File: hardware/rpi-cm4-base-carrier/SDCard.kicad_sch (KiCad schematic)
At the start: 6 parts, among them J6 Micro_SD_Card_Det, U6 RT9742GGJ5

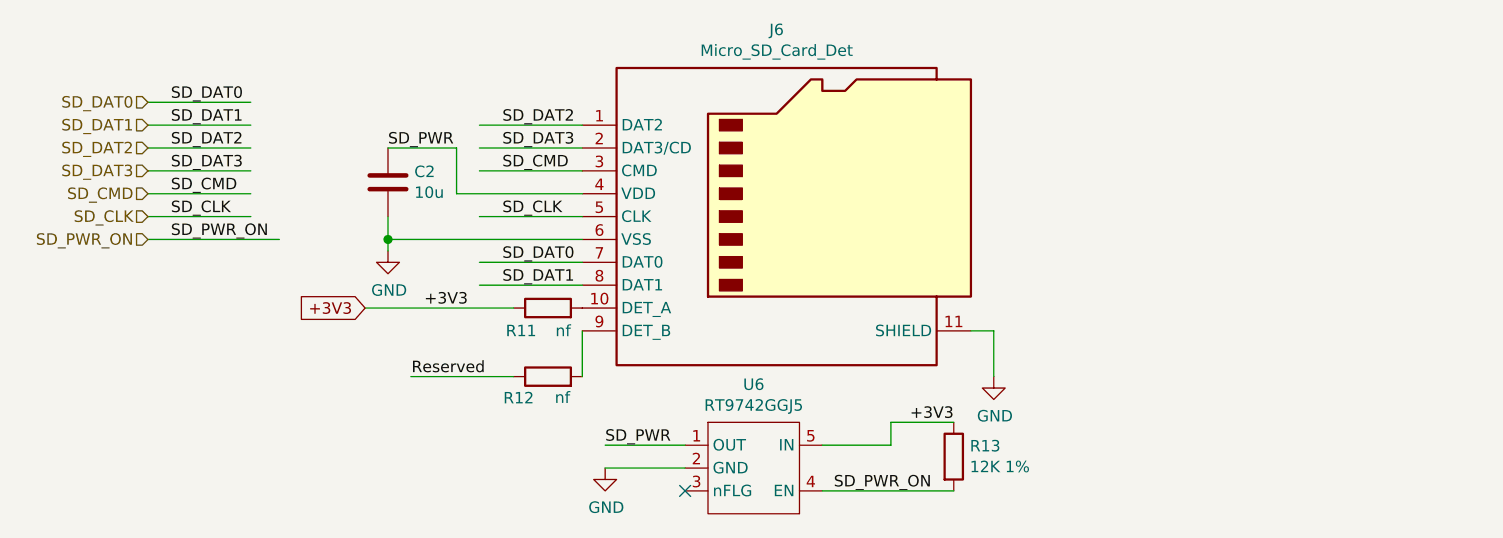
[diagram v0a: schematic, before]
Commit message: routing for some modules progressing quickly, USBHUB mostly complete, thought needed regarding which connectors should be exposed post assembly and which should be for internal use only. LED identifiers and buttons still missing
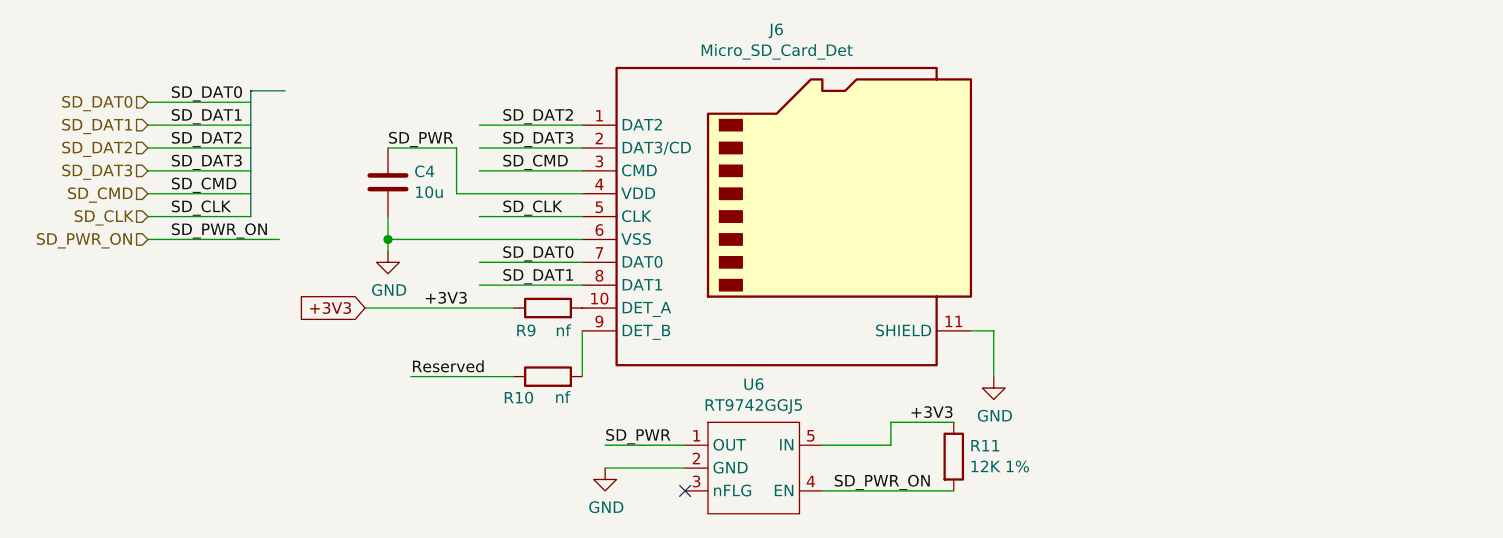
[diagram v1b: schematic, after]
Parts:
- renumbered C2 to C4, R12 to R10, R13 to R11, R11 to R9
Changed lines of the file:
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@@
     (stroke (width 0) (type solid))
+  )
+  (bus (pts (xy 54.61 24.13) (xy 50.8 24.13))
+    (stroke (width 0) (type default))
   )
   (wire (pts (xy 39.37 27.94) (xy 50.8 27.94))
@@
     (stroke (width 0) (type solid))
   )
+  (bus (pts (xy 50.8 24.13) (xy 50.8 38.1))
+    (stroke (width 0) (type default))
+  )
   (label "SD_PWR_ON" (at 41.91 40.64 0) (fields_autoplaced)
     (effects (font (size 1.27 1.27)) (justify left bottom))
@@
     (effects (font (size 1.27 1.27)) (justify right))
   )
+  (netclass_flag "" (length 2.54) (shape round) (at 54.61 24.13 0) (fields_autoplaced)
+    (effects (font (size 1.27 1.27)) (justify left bottom))
+    (property "Netclass" "SD 50R Single" (at 55.499 21.59 0)
+      (effects (font (size 1.27 1.27) italic) (justify left))
+    )
+  )
   (symbol (lib_id "Device:R") (at 83.82 55.88 90) (unit 1)
     (in_bom yes) (on_board yes) (dnp no)
-    (property "Reference" "R12" (at 82.2706 58.2676 90)
+    (property "Reference" "R10" (at 82.2706 58.2676 90)
       (effects (font (size 1.27 1.27)) (justify left))
     )
@@
       (project "rpi-cm4-base-carrier"
         (path "/92c58705-ecb0-498b-b561-44a3f0daad57/26b25ff9-f711-41bc-bcf8-c3ce0c6a0e37"
-          (reference "R12") (unit 1)
+          (reference "R10") (unit 1)
         )
       )
@@
   (symbol (lib_id "power:GND") (at 133.35 55.88 0) (unit 1)
     (in_bom yes) (on_board yes) (dnp no)
-    (property "Reference" "#PWR07" (at 133.35 62.23 0)
+    (property "Reference" "#PWR023" (at 133.35 62.23 0)
       (effects (font (size 1.27 1.27)) hide)
     )
@@
       (project "rpi-cm4-base-carrier"
         (path "/92c58705-ecb0-498b-b561-44a3f0daad57/26b25ff9-f711-41bc-bcf8-c3ce0c6a0e37"
-          (reference "#PWR07") (unit 1)
+          (reference "#PWR023") (unit 1)
         )
       )
@@
   (symbol (lib_id "power:GND") (at 66.04 41.91 0) (unit 1)
     (in_bom yes) (on_board yes) (dnp no)
-    (property "Reference" "#PWR05" (at 66.04 48.26 0)
+    (property "Reference" "#PWR021" (at 66.04 48.26 0)
       (effects (font (size 1.27 1.27)) hide)
     )
@@
       (project "rpi-cm4-base-carrier"
         (path "/92c58705-ecb0-498b-b561-44a3f0daad57/26b25ff9-f711-41bc-bcf8-c3ce0c6a0e37"
-          (reference "#PWR05") (unit 1)
+          (reference "#PWR021") (unit 1)
         )
       )
@@
   (symbol (lib_id "Device:R") (at 83.82 48.26 90) (unit 1)
     (in_bom yes) (on_board yes) (dnp no)
-    (property "Reference" "R11" (at 82.55 50.8 90)
+    (property "Reference" "R9" (at 82.55 50.8 90)
       (effects (font (size 1.27 1.27)) (justify left))
     )
@@
       (project "rpi-cm4-base-carrier"
         (path "/92c58705-ecb0-498b-b561-44a3f0daad57/26b25ff9-f711-41bc-bcf8-c3ce0c6a0e37"
+          (reference "R9") (unit 1)
+        )
+      )
+      (project "CM4IOv5"
+        (path "/e63e39d7-6ac0-4ffd-8aa3-1841a4541b55/00000000-0000-0000-0000-00005cff706a"
+          (reference "R17") (unit 1)
+        )
+      )
+    )
+  )
+  (symbol (lib_id "Device:R") (at 128.905 64.77 0) (unit 1)
+    (in_bom yes) (on_board yes) (dnp no)
+    (property "Reference" "R11" (at 130.683 63.6016 0)
+      (effects (font (size 1.27 1.27)) (justify left))
+    )
+    (property "Value" "12K 1%" (at 130.683 65.913 0)
+      (effects (font (size 1.27 1.27)) (justify left))
+    )
+    (property "Footprint" "Resistor_SMD:R_0402_1005Metric" (at 127.127 64.77 90)
+      (effects (font (size 1.27 1.27)) hide)
+    )
+    (property "Datasheet" "https://fscdn.rohm.com/en/products/databook/datasheet/passive/resistor/chip_resistor/mcr-e.pdf" (at 128.905 64.77 0)
+      (effects (font (size 1.27 1.27)) hide)
+    )
+    (property "Field4" "Farnell" (at 128.905 64.77 0)
+      (effects (font (size 1.27 1.27)) hide)
+    )
+    (property "Field5" "9239367" (at 128.905 64.77 0)
+      (effects (font (size 1.27 1.27)) hide)
+    )
+    (property "Field7" "Rohm" (at 128.905 64.77 0)
+      (effects (font (size 1.27 1.27)) hide)
+    )
+    (property "Field6" "MCR01MZPF1202" (at 128.905 64.77 0)
+      (effects (font (size 1.27 1.27)) hide)
+    )
+    (property "Part Description" "Resistor 12K M1005 1% 63mW" (at 128.905 64.77 0)
+      (effects (font (size 1.27 1.27)) hide)
+    )
+    (pin "1")
+    (pin "2")
+    (instances
+      (project "rpi-cm4-base-carrier"
+        (path "/92c58705-ecb0-498b-b561-44a3f0daad57/26b25ff9-f711-41bc-bcf8-c3ce0c6a0e37"
           (reference "R11") (unit 1)
         )
@@
       (project "CM4IOv5"
         (path "/e63e39d7-6ac0-4ffd-8aa3-1841a4541b55/00000000-0000-0000-0000-00005cff706a"
-          (reference "R17") (unit 1)
-        )
-      )
-    )
-  )
-  (symbol (lib_id "Device:R") (at 128.905 64.77 0) (unit 1)
-    (in_bom yes) (on_board yes) (dnp no)
-    (property "Reference" "R13" (at 130.683 63.6016 0)
-      (effects (font (size 1.27 1.27)) (justify left))
-    )
-    (property "Value" "12K 1%" (at 130.683 65.913 0)
-      (effects (font (size 1.27 1.27)) (justify left))
-    )
-    (property "Footprint" "Resistor_SMD:R_0402_1005Metric" (at 127.127 64.77 90)
-      (effects (font (size 1.27 1.27)) hide)
-    )
-    (property "Datasheet" "https://fscdn.rohm.com/en/products/databook/datasheet/passive/resistor/chip_resistor/mcr-e.pdf" (at 128.905 64.77 0)
-      (effects (font (size 1.27 1.27)) hide)
-    )
-    (property "Field4" "Farnell" (at 128.905 64.77 0)
-      (effects (font (size 1.27 1.27)) hide)
-    )
-    (property "Field5" "9239367" (at 128.905 64.77 0)
-      (effects (font (size 1.27 1.27)) hide)
-    )
-    (property "Field7" "Rohm" (at 128.905 64.77 0)
-      (effects (font (size 1.27 1.27)) hide)
-    )
-    (property "Field6" "MCR01MZPF1202" (at 128.905 64.77 0)
-      (effects (font (size 1.27 1.27)) hide)
-    )
-    (property "Part Description" "Resistor 12K M1005 1% 63mW" (at 128.905 64.77 0)
+          (reference "R29") (unit 1)
+        )
+      )
+    )
+  )
+  (symbol (lib_id "Device:C") (at 66.04 34.29 0) (unit 1)
+    (in_bom yes) (on_board yes) (dnp no)
+    (property "Reference" "C4" (at 68.961 33.1216 0)
+      (effects (font (size 1.27 1.27)) (justify left))
+    )
+    (property "Value" "10u" (at 68.961 35.433 0)
+      (effects (font (size 1.27 1.27)) (justify left))
+    )
+    (property "Footprint" "Capacitor_SMD:C_0805_2012Metric" (at 67.0052 38.1 0)
+      (effects (font (size 1.27 1.27)) hide)
+    )
+    (property "Datasheet" "https://search.murata.co.jp/Ceramy/image/img/A01X/G101/ENG/GRM21BR71A106KA73-01.pdf" (at 66.04 34.29 0)
+      (effects (font (size 1.27 1.27)) hide)
+    )
+    (property "Field5" "490-14381-1-ND" (at 66.04 34.29 0)
+      (effects (font (size 1.27 1.27)) hide)
+    )
+    (property "Field4" "Digikey" (at 66.04 34.29 0)
+      (effects (font (size 1.27 1.27)) hide)
+    )
+    (property "Field6" "GRM21BR71A106KA73L" (at 66.04 34.29 0)
+      (effects (font (size 1.27 1.27)) hide)
+    )
+    (property "Field7" "Murata" (at 66.04 34.29 0)
+      (effects (font (size 1.27 1.27)) hide)
+    )
+    (property "Part Description" "	10uF 10% 10V Ceramic Capacitor X7R 0805 (2012 Metric)" (at 66.04 34.29 0)
+      (effects (font (size 1.27 1.27)) hide)
+    )
+    (property "Field8" "111893011" (at 66.04 34.29 0)
       (effects (font (size 1.27 1.27)) hide)
     )
@@
       (project "rpi-cm4-base-carrier"
         (path "/92c58705-ecb0-498b-b561-44a3f0daad57/26b25ff9-f711-41bc-bcf8-c3ce0c6a0e37"
-          (reference "R13") (unit 1)
-        )
-      )
-      (project "CM4IOv5"
-        (path "/e63e39d7-6ac0-4ffd-8aa3-1841a4541b55/00000000-0000-0000-0000-00005cff706a"
-          (reference "R29") (unit 1)
-        )
-      )
-    )
-  )
-  (symbol (lib_id "Device:C") (at 66.04 34.29 0) (unit 1)
-    (in_bom yes) (on_board yes) (dnp no)
-    (property "Reference" "C2" (at 68.961 33.1216 0)
-      (effects (font (size 1.27 1.27)) (justify left))
-    )
-    (property "Value" "10u" (at 68.961 35.433 0)
-      (effects (font (size 1.27 1.27)) (justify left))
-    )
-    (property "Footprint" "Capacitor_SMD:C_0805_2012Metric" (at 67.0052 38.1 0)
-      (effects (font (size 1.27 1.27)) hide)
-    )
-    (property "Datasheet" "https://search.murata.co.jp/Ceramy/image/img/A01X/G101/ENG/GRM21BR71A106KA73-01.pdf" (at 66.04 34.29 0)
-      (effects (font (size 1.27 1.27)) hide)
-    )
-    (property "Field5" "490-14381-1-ND" (at 66.04 34.29 0)
-      (effects (font (size 1.27 1.27)) hide)
-    )
-    (property "Field4" "Digikey" (at 66.04 34.29 0)
-      (effects (font (size 1.27 1.27)) hide)
-    )
-    (property "Field6" "GRM21BR71A106KA73L" (at 66.04 34.29 0)
-      (effects (font (size 1.27 1.27)) hide)
-    )
-    (property "Field7" "Murata" (at 66.04 34.29 0)
-      (effects (font (size 1.27 1.27)) hide)
-    )
-    (property "Part Description" "	10uF 10% 10V Ceramic Capacitor X7R 0805 (2012 Metric)" (at 66.04 34.29 0)
-      (effects (font (size 1.27 1.27)) hide)
-    )
-    (property "Field8" "111893011" (at 66.04 34.29 0)
-      (effects (font (size 1.27 1.27)) hide)
-    )
-    (pin "1")
-    (pin "2")
-    (instances
-      (project "rpi-cm4-base-carrier"
-        (path "/92c58705-ecb0-498b-b561-44a3f0daad57/26b25ff9-f711-41bc-bcf8-c3ce0c6a0e37"
-          (reference "C2") (unit 1)
+          (reference "C4") (unit 1)
         )
       )
@@
   (symbol (lib_id "power:GND") (at 90.17 66.04 0) (unit 1)
     (in_bom yes) (on_board yes) (dnp no)
-    (property "Reference" "#PWR06" (at 90.17 72.39 0)
+    (property "Reference" "#PWR022" (at 90.17 72.39 0)
       (effects (font (size 1.27 1.27)) hide)
     )
@@
       (project "rpi-cm4-base-carrier"
         (path "/92c58705-ecb0-498b-b561-44a3f0daad57/26b25ff9-f711-41bc-bcf8-c3ce0c6a0e37"
-          (reference "#PWR06") (unit 1)
-        )
-      )
+          (reference "#PWR022") (unit 1)
+        )
+      )

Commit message: started final placement of blocks, realised ESD suppression devices cannot be manufactured with JLC, need to switch part
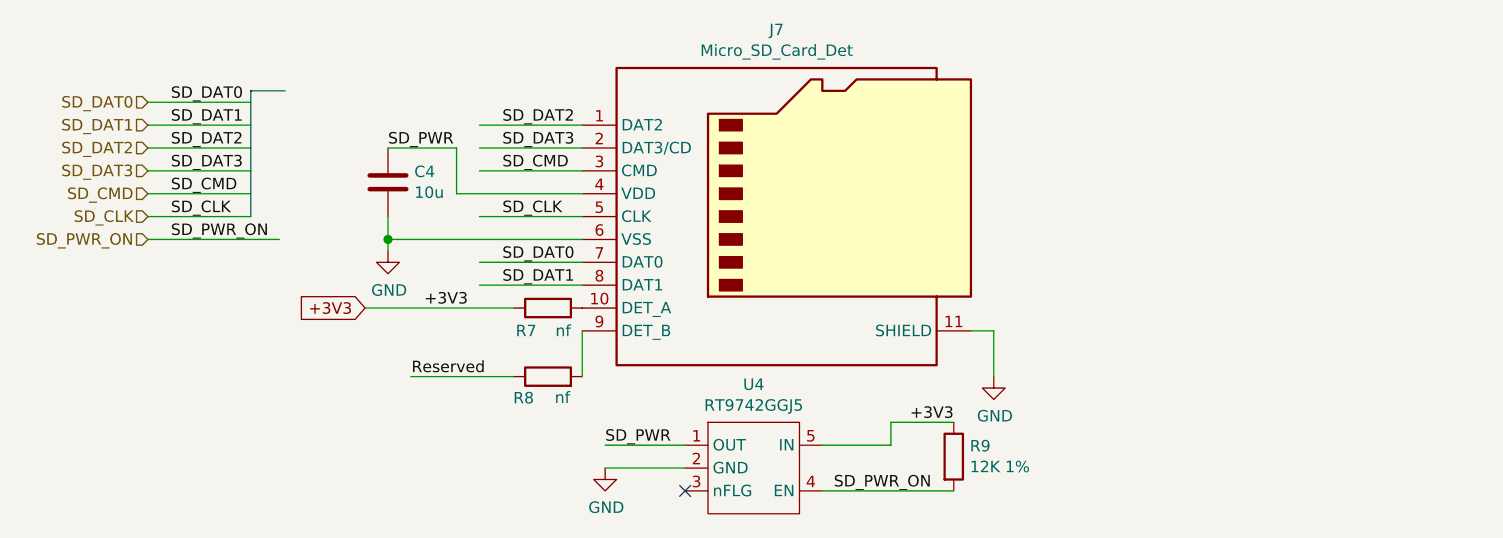
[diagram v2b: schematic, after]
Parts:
- renumbered J6 to J7, R9 to R7, R10 to R8, R11 to R9, U6 to U4
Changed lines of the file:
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@@
   (symbol (lib_id "Device:R") (at 83.82 55.88 90) (unit 1)
     (in_bom yes) (on_board yes) (dnp no)
-    (property "Reference" "R10" (at 82.2706 58.2676 90)
+    (property "Reference" "R8" (at 82.2706 58.2676 90)
       (effects (font (size 1.27 1.27)) (justify left))
     )
@@
       (project "rpi-cm4-base-carrier"
         (path "/92c58705-ecb0-498b-b561-44a3f0daad57/26b25ff9-f711-41bc-bcf8-c3ce0c6a0e37"
-          (reference "R10") (unit 1)
+          (reference "R8") (unit 1)
         )
       )
@@
   (symbol (lib_id "Connector:Micro_SD_Card_Det") (at 110.49 38.1 0) (unit 1)
     (in_bom yes) (on_board yes) (dnp no)
-    (property "Reference" "J6" (at 109.22 17.3482 0)
+    (property "Reference" "J7" (at 109.22 17.3482 0)
       (effects (font (size 1.27 1.27)))
     )
@@
       (project "rpi-cm4-base-carrier"
         (path "/92c58705-ecb0-498b-b561-44a3f0daad57/26b25ff9-f711-41bc-bcf8-c3ce0c6a0e37"
-          (reference "J6") (unit 1)
-        )
-      )
-      (project "CM4IOv5"
-        (path "/e63e39d7-6ac0-4ffd-8aa3-1841a4541b55/00000000-0000-0000-0000-00005cff706a"
           (reference "J7") (unit 1)
         )
       )
+      (project "CM4IOv5"
+        (path "/e63e39d7-6ac0-4ffd-8aa3-1841a4541b55/00000000-0000-0000-0000-00005cff706a"
+          (reference "J7") (unit 1)
+        )
+      )
     )
   )
   (symbol (lib_id "power:GND") (at 133.35 55.88 0) (unit 1)
     (in_bom yes) (on_board yes) (dnp no)
-    (property "Reference" "#PWR023" (at 133.35 62.23 0)
+    (property "Reference" "#PWR022" (at 133.35 62.23 0)
       (effects (font (size 1.27 1.27)) hide)
     )
@@
       (project "rpi-cm4-base-carrier"
         (path "/92c58705-ecb0-498b-b561-44a3f0daad57/26b25ff9-f711-41bc-bcf8-c3ce0c6a0e37"
-          (reference "#PWR023") (unit 1)
+          (reference "#PWR022") (unit 1)
         )
       )
@@
   (symbol (lib_id "power:GND") (at 66.04 41.91 0) (unit 1)
     (in_bom yes) (on_board yes) (dnp no)
-    (property "Reference" "#PWR021" (at 66.04 48.26 0)
+    (property "Reference" "#PWR020" (at 66.04 48.26 0)
       (effects (font (size 1.27 1.27)) hide)
     )
@@
       (project "rpi-cm4-base-carrier"
         (path "/92c58705-ecb0-498b-b561-44a3f0daad57/26b25ff9-f711-41bc-bcf8-c3ce0c6a0e37"
-          (reference "#PWR021") (unit 1)
+          (reference "#PWR020") (unit 1)
         )
       )
@@
   (symbol (lib_id "CM4IO:RT9742GGJ5") (at 107.95 73.66 0) (unit 1)
     (in_bom yes) (on_board yes) (dnp no)
-    (property "Reference" "U6" (at 106.68 56.769 0)
+    (property "Reference" "U4" (at 106.68 56.769 0)
       (effects (font (size 1.27 1.27)))
     )
@@
       (project "rpi-cm4-base-carrier"
         (path "/92c58705-ecb0-498b-b561-44a3f0daad57/26b25ff9-f711-41bc-bcf8-c3ce0c6a0e37"
-          (reference "U6") (unit 1)
+          (reference "U4") (unit 1)
         )
       )
@@
   (symbol (lib_id "Device:R") (at 83.82 48.26 90) (unit 1)
     (in_bom yes) (on_board yes) (dnp no)
-    (property "Reference" "R9" (at 82.55 50.8 90)
+    (property "Reference" "R7" (at 82.55 50.8 90)
       (effects (font (size 1.27 1.27)) (justify left))
     )
@@
       (project "rpi-cm4-base-carrier"
         (path "/92c58705-ecb0-498b-b561-44a3f0daad57/26b25ff9-f711-41bc-bcf8-c3ce0c6a0e37"
+          (reference "R7") (unit 1)
+        )
+      )
+      (project "CM4IOv5"
+        (path "/e63e39d7-6ac0-4ffd-8aa3-1841a4541b55/00000000-0000-0000-0000-00005cff706a"
+          (reference "R17") (unit 1)
+        )
+      )
+    )
+  )
+  (symbol (lib_id "Device:R") (at 128.905 64.77 0) (unit 1)
+    (in_bom yes) (on_board yes) (dnp no)
+    (property "Reference" "R9" (at 130.683 63.6016 0)
+      (effects (font (size 1.27 1.27)) (justify left))
+    )
+    (property "Value" "12K 1%" (at 130.683 65.913 0)
+      (effects (font (size 1.27 1.27)) (justify left))
+    )
+    (property "Footprint" "Resistor_SMD:R_0402_1005Metric" (at 127.127 64.77 90)
+      (effects (font (size 1.27 1.27)) hide)
+    )
+    (property "Datasheet" "https://fscdn.rohm.com/en/products/databook/datasheet/passive/resistor/chip_resistor/mcr-e.pdf" (at 128.905 64.77 0)
+      (effects (font (size 1.27 1.27)) hide)
+    )
+    (property "Field4" "Farnell" (at 128.905 64.77 0)
+      (effects (font (size 1.27 1.27)) hide)
+    )
+    (property "Field5" "9239367" (at 128.905 64.77 0)
+      (effects (font (size 1.27 1.27)) hide)
+    )
+    (property "Field7" "Rohm" (at 128.905 64.77 0)
+      (effects (font (size 1.27 1.27)) hide)
+    )
+    (property "Field6" "MCR01MZPF1202" (at 128.905 64.77 0)
+      (effects (font (size 1.27 1.27)) hide)
+    )
+    (property "Part Description" "Resistor 12K M1005 1% 63mW" (at 128.905 64.77 0)
+      (effects (font (size 1.27 1.27)) hide)
+    )
+    (pin "1")
+    (pin "2")
+    (instances
+      (project "rpi-cm4-base-carrier"
+        (path "/92c58705-ecb0-498b-b561-44a3f0daad57/26b25ff9-f711-41bc-bcf8-c3ce0c6a0e37"
           (reference "R9") (unit 1)
         )
@@
       (project "CM4IOv5"
         (path "/e63e39d7-6ac0-4ffd-8aa3-1841a4541b55/00000000-0000-0000-0000-00005cff706a"
-          (reference "R17") (unit 1)
-        )
-      )
-    )
-  )
-  (symbol (lib_id "Device:R") (at 128.905 64.77 0) (unit 1)
-    (in_bom yes) (on_board yes) (dnp no)
-    (property "Reference" "R11" (at 130.683 63.6016 0)
-      (effects (font (size 1.27 1.27)) (justify left))
-    )
-    (property "Value" "12K 1%" (at 130.683 65.913 0)
-      (effects (font (size 1.27 1.27)) (justify left))
-    )
-    (property "Footprint" "Resistor_SMD:R_0402_1005Metric" (at 127.127 64.77 90)
-      (effects (font (size 1.27 1.27)) hide)
-    )
-    (property "Datasheet" "https://fscdn.rohm.com/en/products/databook/datasheet/passive/resistor/chip_resistor/mcr-e.pdf" (at 128.905 64.77 0)
-      (effects (font (size 1.27 1.27)) hide)
-    )
-    (property "Field4" "Farnell" (at 128.905 64.77 0)
-      (effects (font (size 1.27 1.27)) hide)
-    )
-    (property "Field5" "9239367" (at 128.905 64.77 0)
-      (effects (font (size 1.27 1.27)) hide)
-    )
-    (property "Field7" "Rohm" (at 128.905 64.77 0)
-      (effects (font (size 1.27 1.27)) hide)
-    )
-    (property "Field6" "MCR01MZPF1202" (at 128.905 64.77 0)
-      (effects (font (size 1.27 1.27)) hide)
-    )
-    (property "Part Description" "Resistor 12K M1005 1% 63mW" (at 128.905 64.77 0)
-      (effects (font (size 1.27 1.27)) hide)
-    )
-    (pin "1")
-    (pin "2")
-    (instances
-      (project "rpi-cm4-base-carrier"
-        (path "/92c58705-ecb0-498b-b561-44a3f0daad57/26b25ff9-f711-41bc-bcf8-c3ce0c6a0e37"
-          (reference "R11") (unit 1)
-        )
-      )
-      (project "CM4IOv5"
-        (path "/e63e39d7-6ac0-4ffd-8aa3-1841a4541b55/00000000-0000-0000-0000-00005cff706a"
           (reference "R29") (unit 1)
         )
@@
   (symbol (lib_id "power:GND") (at 90.17 66.04 0) (unit 1)
     (in_bom yes) (on_board yes) (dnp no)
-    (property "Reference" "#PWR022" (at 90.17 72.39 0)
+    (property "Reference" "#PWR021" (at 90.17 72.39 0)
       (effects (font (size 1.27 1.27)) hide)
     )
@@
       (project "rpi-cm4-base-carrier"
         (path "/92c58705-ecb0-498b-b561-44a3f0daad57/26b25ff9-f711-41bc-bcf8-c3ce0c6a0e37"
-          (reference "#PWR022") (unit 1)
-        )
-      )
+          (reference "#PWR021") (unit 1)
+        )
+      )
